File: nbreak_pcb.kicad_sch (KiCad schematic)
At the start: 27 parts, among them J1 Conn_01x16, J2 Conn_01x05, Q1 BSS138, Q2 BSS138, U1 MAX485E, U2 MAX485E

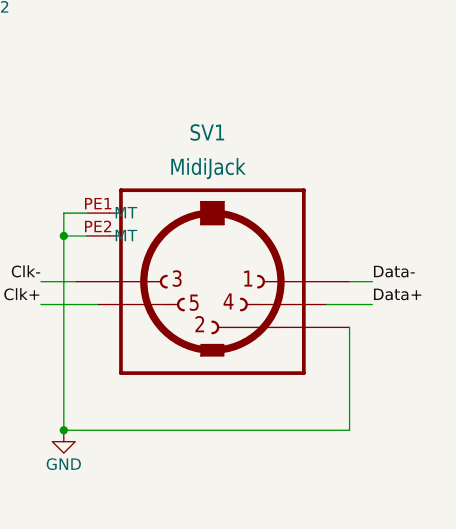
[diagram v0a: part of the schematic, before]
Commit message: Fixed data polarity at DIN socket
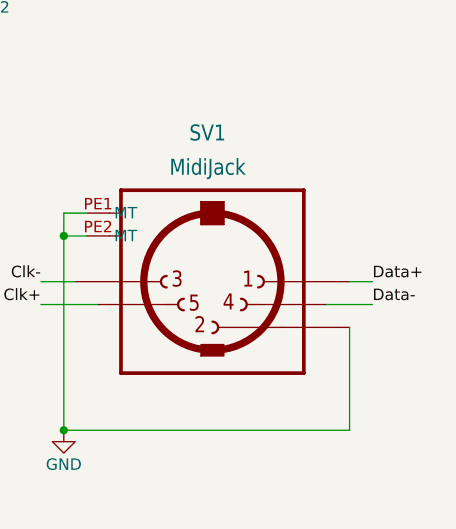
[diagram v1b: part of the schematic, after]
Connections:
- net Data+: now also SV1.1; no longer SV1.4
- net Data-: now also SV1.4; no longer SV1.1
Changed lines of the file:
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@@
 	)
 	(label "Data+"
-		(at 223.52 113.03 0)
+		(at 223.52 110.49 0)
 		(effects
 			(font
@@
 	)
 	(label "Data-"
-		(at 223.52 110.49 0)
+		(at 223.52 113.03 0)
 		(effects
 			(font

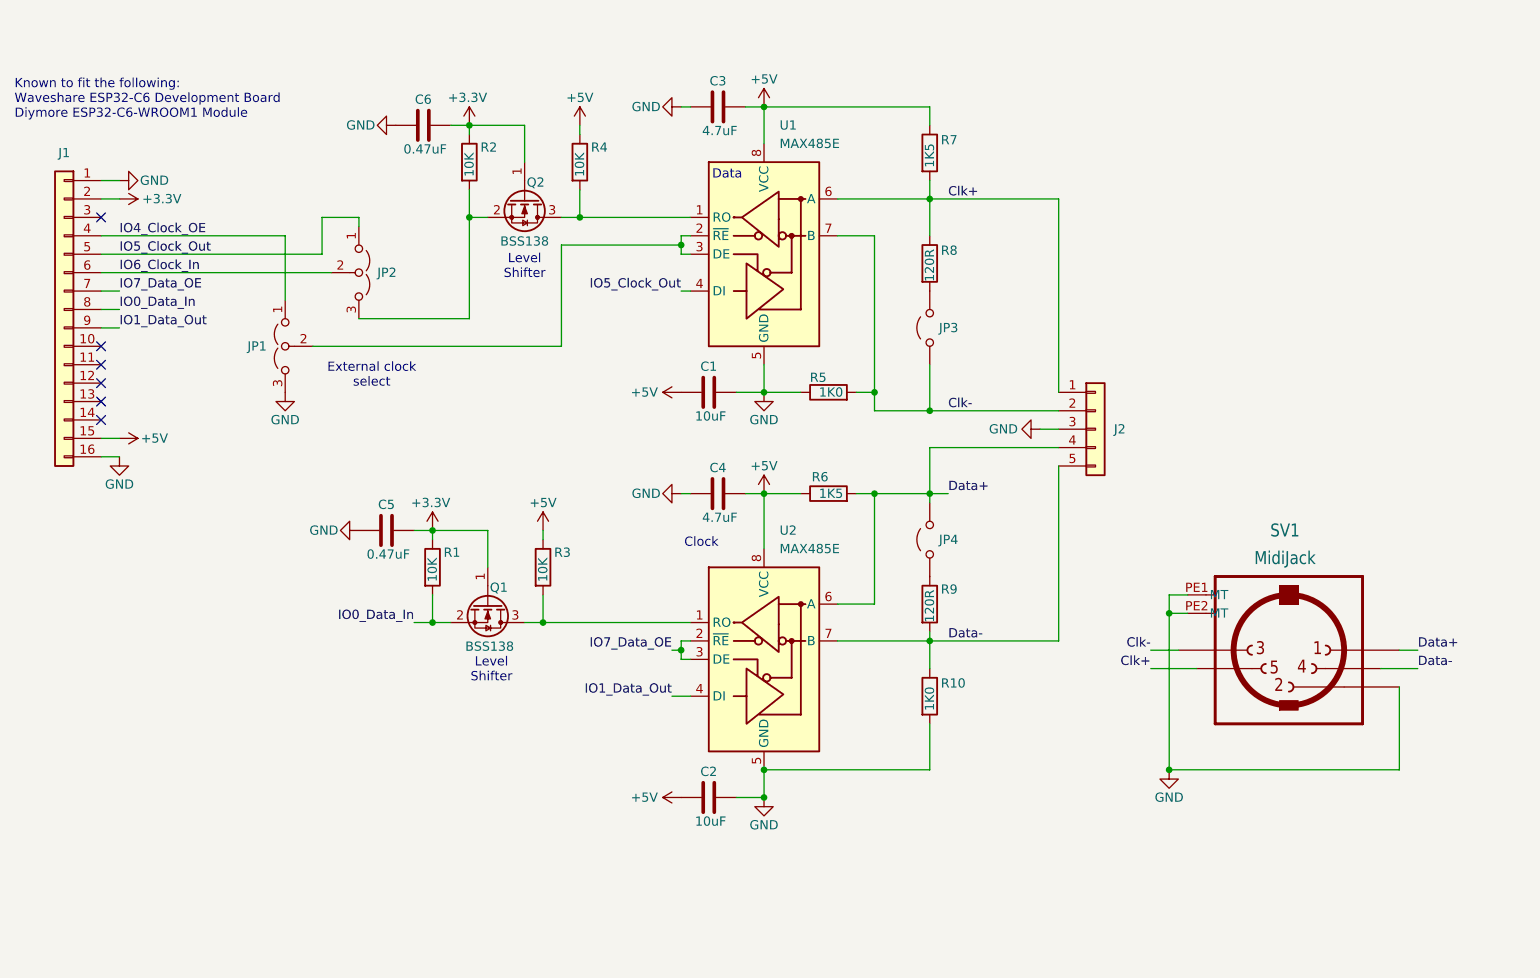
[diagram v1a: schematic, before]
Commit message: Simplified clock and terminator selection
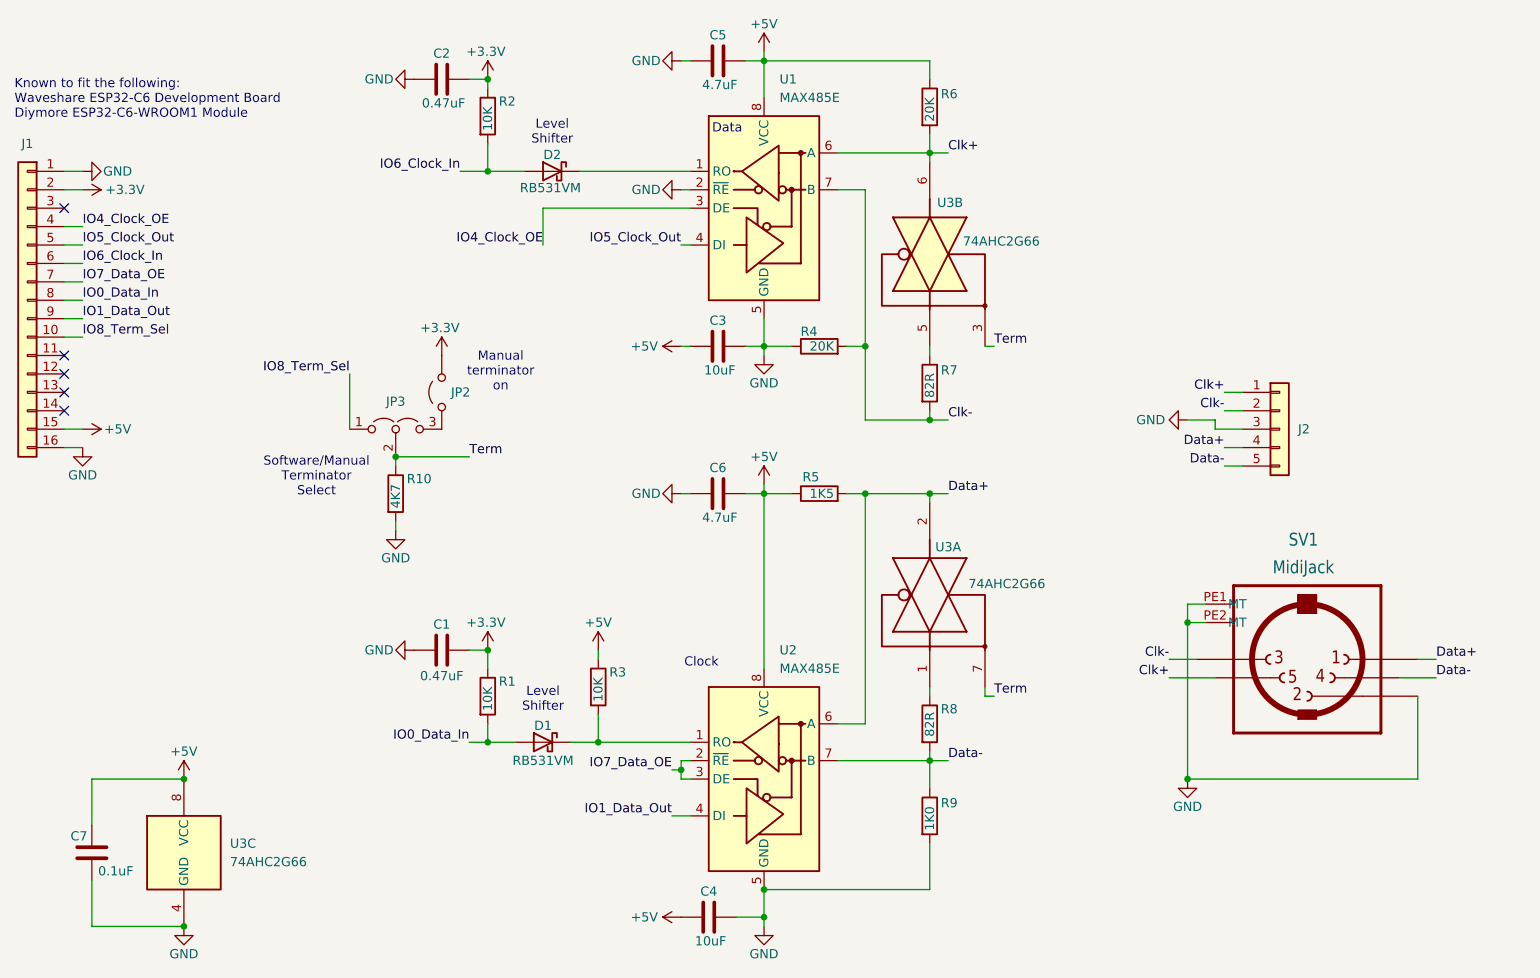
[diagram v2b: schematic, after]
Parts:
- removed JP1, JP2: Jumper_3_Open, Connector_PinHeader_2.54mm:PinHeader_1x03_P2.54mm_Vertical, symbol Jumper:Jumper_3_Open
- removed JP4: Jumper_2_Open, Connector_PinHeader_2.54mm:PinHeader_1x02_P2.54mm_Vertical, symbol Jumper:Jumper_2_Open
- removed Q1, Q2: BSS138, Package_TO_SOT_SMD:SOT-23, symbol Transistor_FET:BSS138
- removed R4: 10K, Resistor_SMD:R_0805_2012Metric_Pad1.20x1.40mm_HandSolder, symbol Device:R
- added C7: 0.1uF, Capacitor_SMD:C_0603_1608Metric_Pad1.08x0.95mm_HandSolder, symbol Device:C
- added D1, D2: RB531VM, Diode_SMD:D_SOD-323F, symbol Device:D_Schottky
- added JP3: Jumper_3_Open, Jumper:SolderJumper-3_P1.3mm_Open_RoundedPad1.0x1.5mm, symbol Jumper:Jumper_3_Open
- added R10: 4K7, Resistor_SMD:R_0805_2012Metric_Pad1.20x1.40mm_HandSolder, symbol Device:R
- added U3: 74AHC2G66, Package_SO:TSSOP-8_3x3mm_P0.65mm, symbol 74xGxx:74AUC2G66
- R4: renamed from R5; value 1K0 -> 20K
- R6: renamed from R7; value 1K5 -> 20K
- R7: renamed from R8; value 120R -> 82R
- R8: renamed from R9; value 120R -> 82R
- renumbered C5 to C1, C6 to C2, C1 to C3, C2 to C4, C3 to C5, C4 to C6, JP3 to JP2, R6 to R5, R10 to R9
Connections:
- net +3.3V: now also JP2.2 (B)
- net +5V: now also C7.2, U3.8 (VCC)
- net Clk+: now also U3.6; no longer R7.1
- net Clk-: now also R7.2; no longer JP2.1 (A)
- net Data+: now also U3.2
- net GND: now also U1.2 (~{RE}), C7.1, R10.2, U3.4 (GND)
- net IO0_Data_In: now also D1.2 (A)
- net IO4_Clock_OE: now also U1.3 (DE)
- net IO6_Clock_In: now also R2.2, D2.2 (A)
- net at R3.2, U2.1 (RO): now also D1.1 (K)
- net at R8.1: now also U3.1
- net at U1.1 (RO): now also D2.1 (K)
- net IO8_Term_Sel: now reaches J1.10 (Pin_10)
- net IO8_Term_Sel: now also JP3.1 (A)
- new net: R7.1, U3.5
- new net: JP2.1 (A), JP3.3 (B)
- new net Term: JP3.2 (C), R10.1, U3.3, U3.7
- no-connect marks 6 -> 5
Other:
- note added: "Manual terminator on"
- note added: "Software/Manual Terminator Select"
- note removed: "External clock select"
- moved on the sheet: C1, C2, C3, C4, C5, J1, J2, JP2, R1, R2, R3, R4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

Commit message: Added activity indicator LEDs
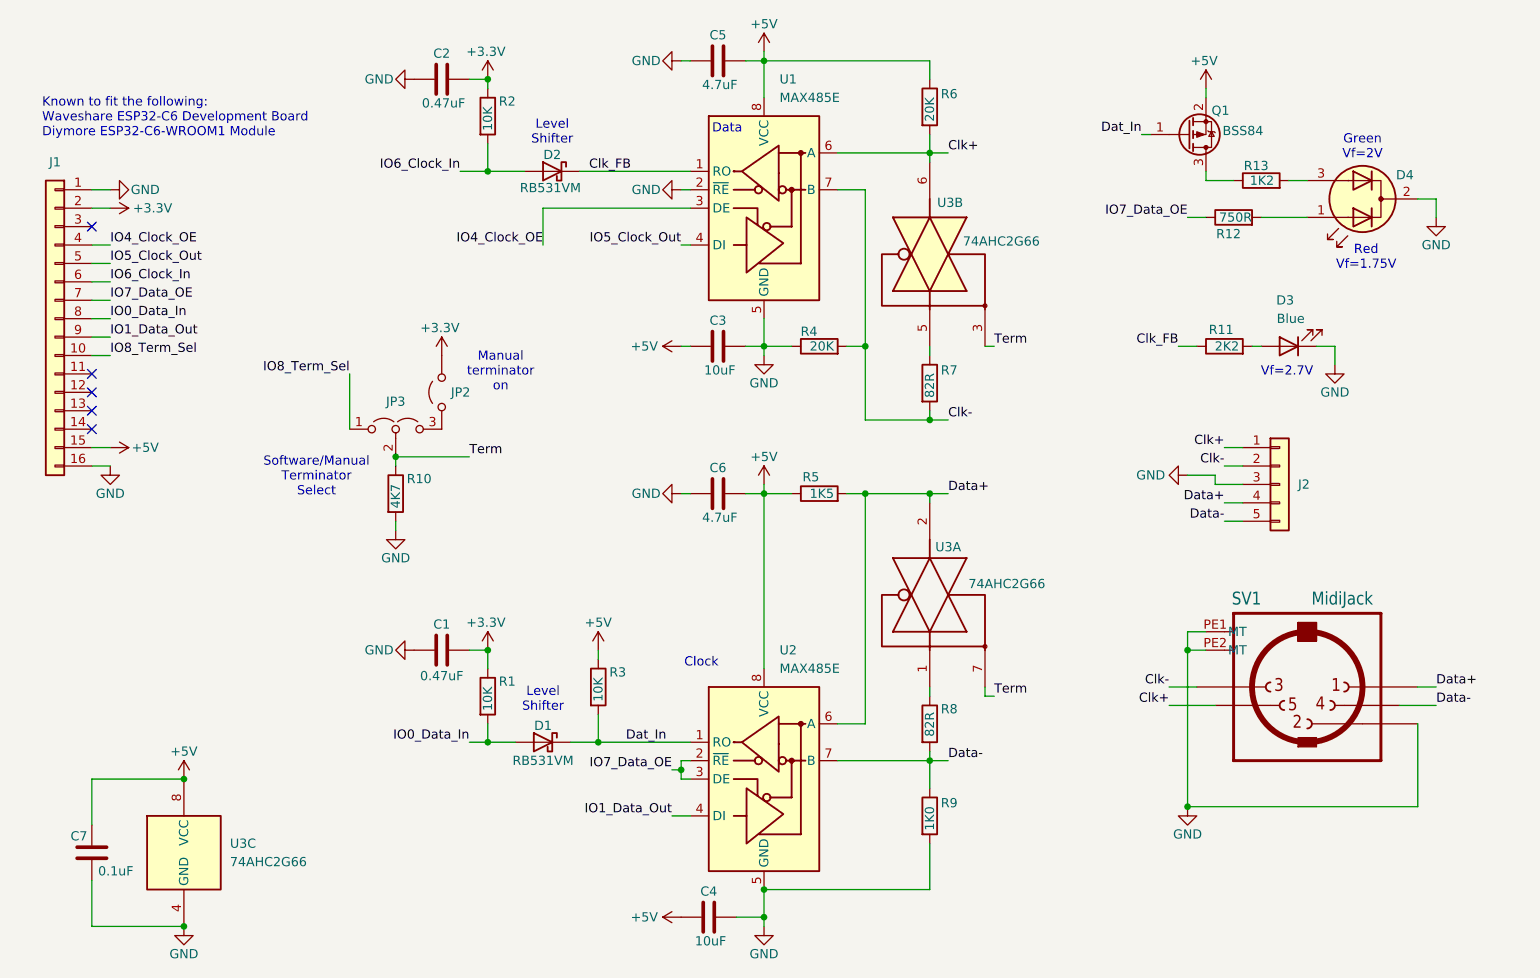
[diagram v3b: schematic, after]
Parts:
- added D3: Blue, LED_THT:LED_D3.0mm, symbol Device:LED
- added D4: LED_Dual_AAK, LED_THT:LED_D3.0mm-3, symbol Device:LED_Dual_AKA
- added Q1: BSS84, Package_TO_SOT_SMD:SOT-23, symbol Transistor_FET:BSS84
- added R11: 2K2, Resistor_SMD:R_0805_2012Metric_Pad1.20x1.40mm_HandSolder, symbol Device:R
- added R12: 750R, Resistor_SMD:R_0805_2012Metric_Pad1.20x1.40mm_HandSolder, symbol Device:R
- added R13: 1K2, Resistor_SMD:R_0805_2012Metric_Pad1.20x1.40mm_HandSolder, symbol Device:R
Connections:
- net +5V: now also Q1.2 (S)
- net GND: now also D3.1 (K), D4.2 (K)
- net IO7_Data_OE: now also R12.1
- net Clk_FB: now reaches D2.1 (K), U1.1 (RO)
- net Clk_FB: now also R11.1
- net Dat_In: now reaches D1.1 (K), R3.2, U2.1 (RO)
- net Dat_In: now also Q1.1 (G)
- new net: D4.1 (A1), R12.2
- new net: D3.2 (A), R11.2
- new net: Q1.3 (D), R13.1
- new net: D4.3 (A2), R13.2
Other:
- note added: "Green Vf=2V"
- note added: "Red Vf=1.75V"
- note added: "Vf=2.7V"
- moved on the sheet: J1, J2, SV1

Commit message: Updates for version 2, following construction of first prototype
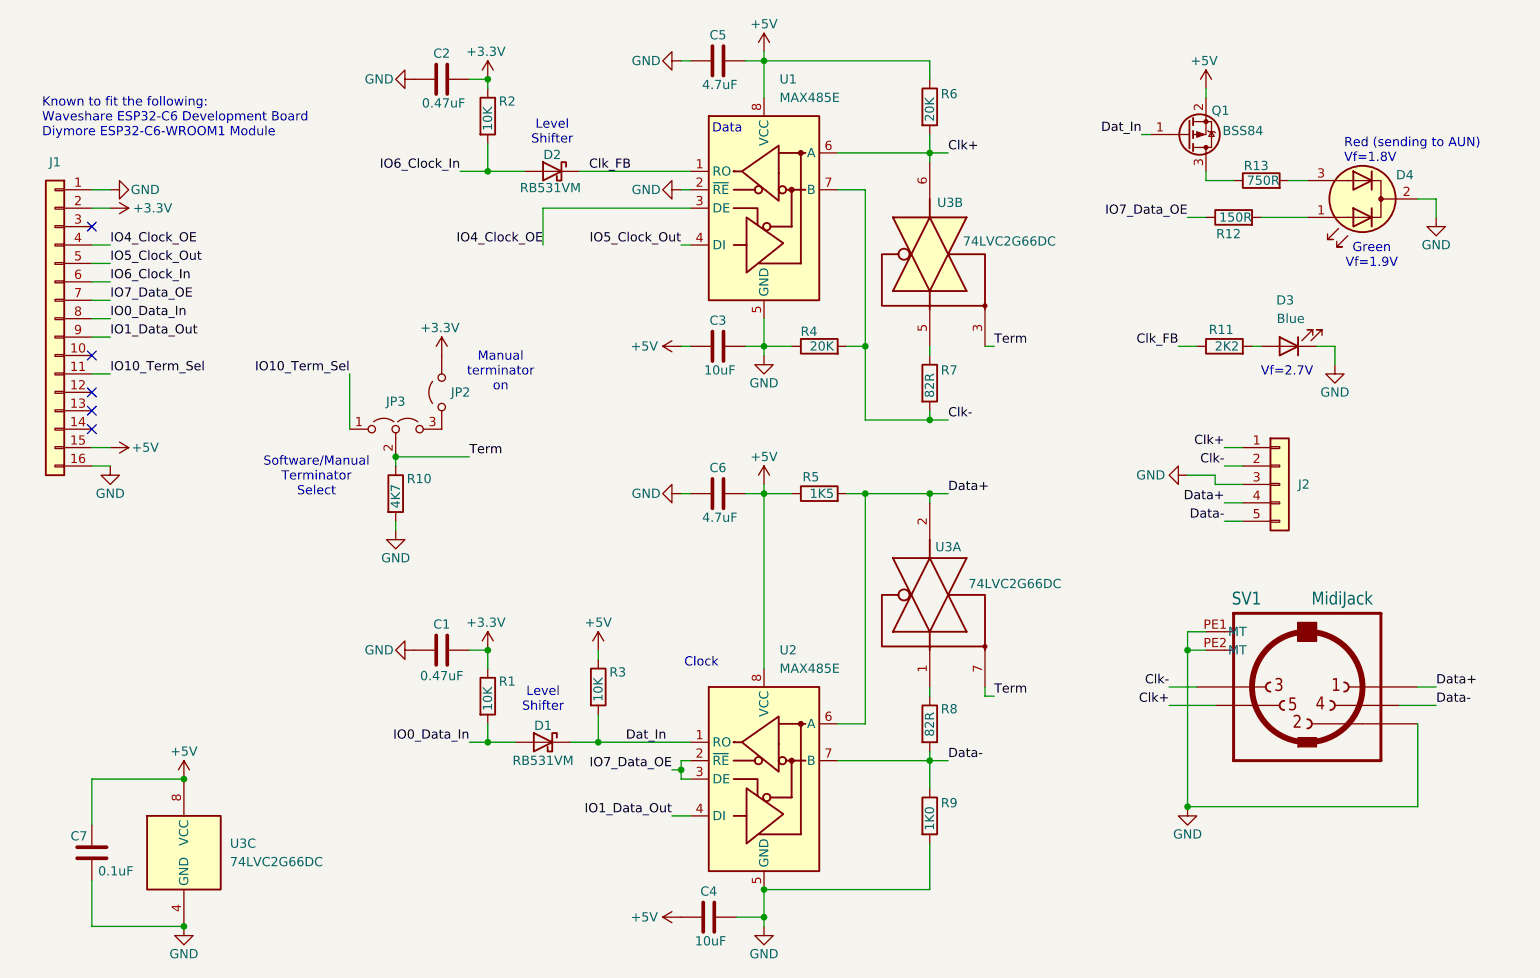
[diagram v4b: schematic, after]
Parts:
- R12: value 750R -> 150R
- R13: value 1K2 -> 750R
- U3: value 74AHC2G66 -> 74LVC2G66DC; footprint Package_SO:TSSOP-8_3x3mm_P0.65mm -> Package_SO:VSSOP-8_2.3x2mm_P0.5mm
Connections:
- net IO10_Term_Sel: now reaches J1.11 (Pin_11)
- net IO10_Term_Sel: now also JP3.1 (A)
- net IO8_Term_Sel: no longer names the net of J1.10 (Pin_10)
- net IO8_Term_Sel: no longer JP3.1 (A)
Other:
- note added: "Green Vf=1.9V"
- note added: "Red (sending to AUN) Vf=1.8V"
- note removed: "Green Vf=2V"
- note removed: "Red Vf=1.75V"
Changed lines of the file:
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@@
 		(rev "1.12")
 	)
-	(text "Red\nVf=1.75V"
+	(text "Red (sending to AUN)\nVf=1.8V"
 		(exclude_from_sim no)
-		(at 216.408 56.388 0)
+		(at 213.36 41.656 0)
 		(effects
 			(font
 				(size 1.27 1.27)
 			)
+			(justify left)
 		)
 	)
@@
 		)
 	)
-	(text "Green\nVf=2V"
+	(text "Green\nVf=1.9V"
 		(exclude_from_sim no)
-		(at 215.9 41.148 0)
+		(at 217.17 56.134 0)
 		(effects
 			(font
@@
 	)
 	(no_connect
-		(at 40.64 72.39)
+		(at 40.64 52.07)
 	)
 	(no_connect
-		(at 40.64 52.07)
+		(at 40.64 69.85)
 	)
 	(no_connect
@@
 	(wire
 		(pts
+			(xy 40.64 72.39) (xy 43.18 72.39)
+		)
+		(stroke
+			(width 0)
+			(type default)
+		)
+	)
+	(wire
+		(pts
 			(xy 190.5 68.58) (xy 193.04 68.58)
 		)
@@
 	(wire
 		(pts
-			(xy 40.64 69.85) (xy 43.18 69.85)
-		)
-		(stroke
-			(width 0)
-			(type default)
-		)
-	)
-	(wire
-		(pts
 			(xy 120.65 127) (xy 121.92 127)
 		)
@@
 		)
 	)
+	(label "IO10_Term_Sel"
+		(at 76.2 72.39 180)
+		(effects
+			(font
+				(size 1.27 1.27)
+			)
+			(justify right bottom)
+		)
+	)
 	(label "IO6_Clock_In"
 		(at 43.18 59.69 0)
@@
 		)
 	)
-	(label "IO8_Term_Sel"
-		(at 43.18 69.85 0)
+	(label "IO10_Term_Sel"
+		(at 43.18 72.39 0)
 		(effects
 			(font
@@
 		)
 	)
-	(label "IO8_Term_Sel"
-		(at 76.2 72.39 180)
-		(effects
-			(font
-				(size 1.27 1.27)
-			)
-			(justify right bottom)
-		)
-	)
 	(label "IO1_Data_Out"
 		(at 43.18 67.31 0)
@@
 			)
 		)
-		(property "Value" "750R"
+		(property "Value" "150R"
 			(at 200.66 50.8 90)
 			(effects
@@
 			)
 		)
-		(property "Value" "74AHC2G66"
+		(property "Value" "74LVC2G66DC"
 			(at 59.69 139.6999 0)
 			(effects
@@
 			)
 		)
-		(property "Footprint" "Package_SO:TSSOP-8_3x3mm_P0.65mm"
+		(property "Footprint" "Package_SO:VSSOP-8_2.3x2mm_P0.5mm"
 			(at 53.34 138.43 0)
 			(effects
@@
 			)
 		)
-		(property "Value" "74AHC2G66"
+		(property "Value" "74LVC2G66DC"
 			(at 160.782 54.102 90)
 			(effects
@@
 			)
 		)
-		(property "Footprint" "Package_SO:TSSOP-8_3x3mm_P0.65mm"
+		(property "Footprint" "Package_SO:VSSOP-8_2.3x2mm_P0.5mm"
 			(at 156.21 55.88 0)
 			(effects
@@
 			)
 		)
-		(property "Value" "74AHC2G66"
+		(property "Value" "74LVC2G66DC"
 			(at 161.544 101.346 90)
 			(effects
@@
 			)
 		)
-		(property "Footprint" "Package_SO:TSSOP-8_3x3mm_P0.65mm"
+		(property "Footprint" "Package_SO:VSSOP-8_2.3x2mm_P0.5mm"
 			(at 156.21 102.87 0)
 			(effects
@@
 			)
 		)
-		(property "Value" "1K2"
-			(at 203.708 45.72 90)
+		(property "Value" "750R"
+			(at 204.47 45.72 90)
 			(effects
 				(font
